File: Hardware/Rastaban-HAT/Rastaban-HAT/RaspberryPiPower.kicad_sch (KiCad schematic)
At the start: 12 parts, among them IC2 BCM53DS, Q3 DMG2305UX-7, U5 LM2596S -5.0

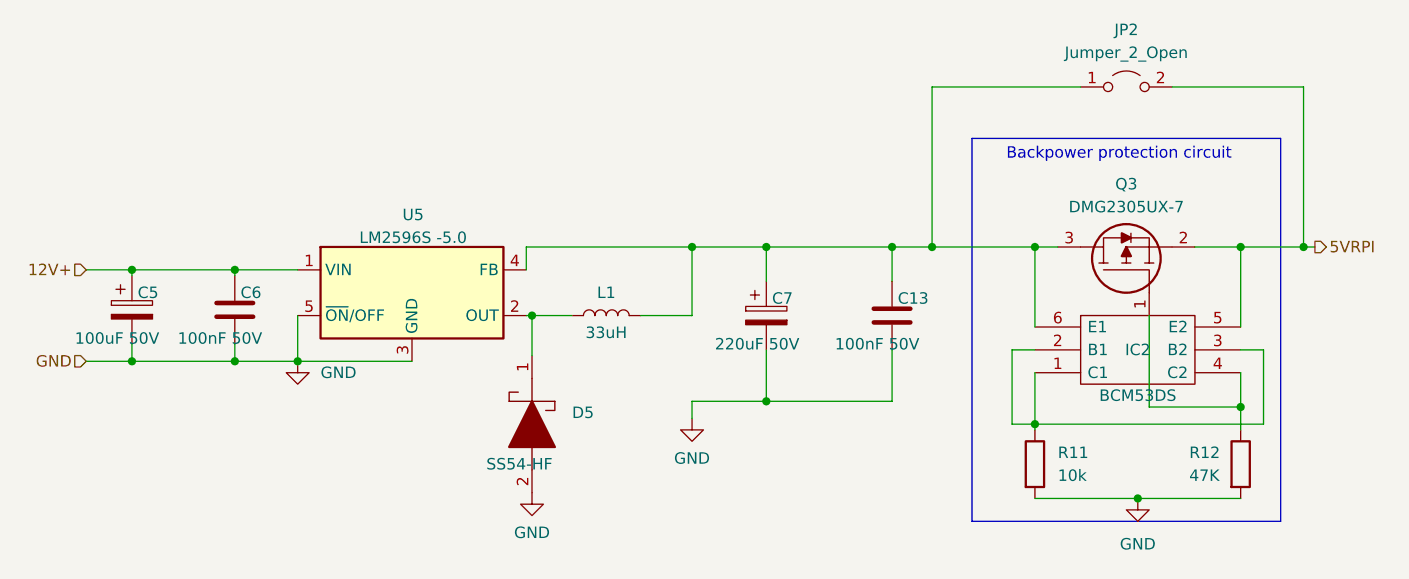
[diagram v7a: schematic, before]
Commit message: worked on PCB and schematic designs
many small changes and some big schematic changes (motors)
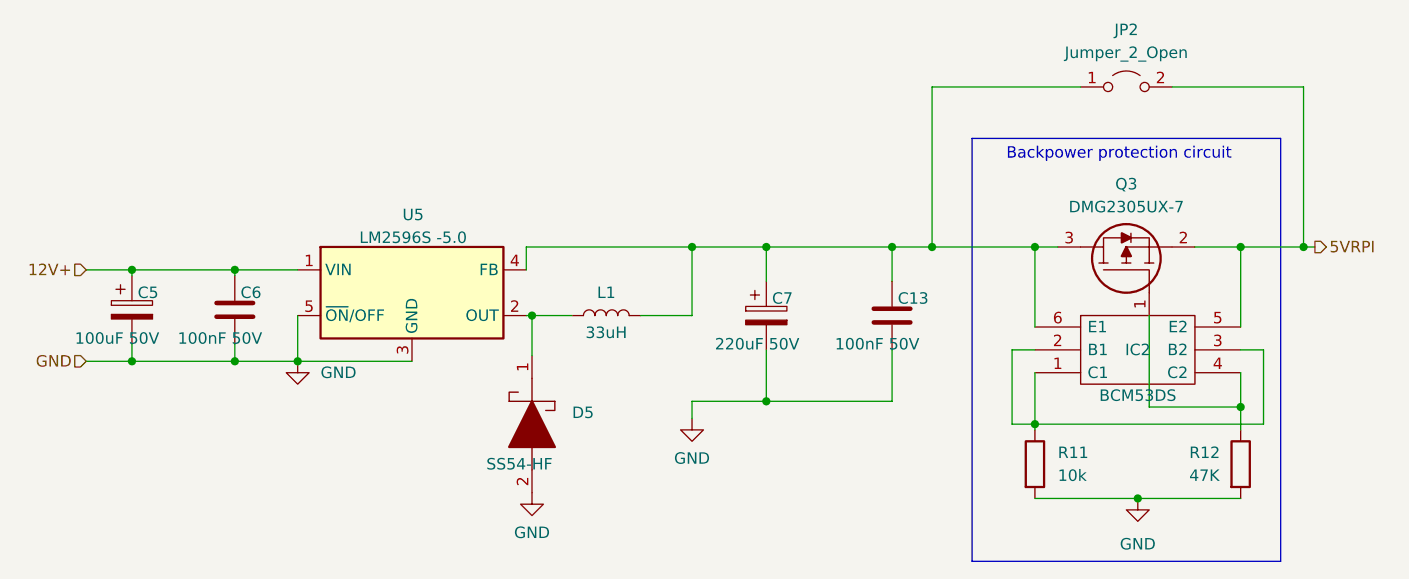
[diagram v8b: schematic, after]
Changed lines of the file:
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@@
   (title_block
     (title "Rastaban-HAT")
-    (date "2022-12-08")
-    (rev "1.5")
+    (date "2022-12-13")
+    (rev "1.6")
     (company "HAN")
     (comment 1 "Casper R. Tak")
@@
     (stroke (width 0) (type default) (color 0 0 0 0))
   )
-  (polyline (pts (xy 132.08 46.355) (xy 132.08 88.9))
+  (polyline (pts (xy 132.08 46.355) (xy 132.08 93.345))
     (stroke (width 0) (type default) (color 0 0 0 0))
   )
@@
     (stroke (width 0) (type default) (color 0 0 0 0))
   )
-  (polyline (pts (xy 166.37 88.9) (xy 132.08 88.9))
+  (polyline (pts (xy 166.37 93.345) (xy 132.08 93.345))
     (stroke (width 0) (type default) (color 0 0 0 0))
   )
@@
     (stroke (width 0) (type default) (color 0 0 0 0))
   )
-  (polyline (pts (xy 166.37 46.355) (xy 166.37 88.9))
-    (stroke (width 0) (type default) (color 0 0 0 0))
-  )
+  (polyline (pts (xy 166.37 46.355) (xy 166.37 93.345))
+    (stroke (width 0) (type default) (color 0 0 0 0))
+  )
